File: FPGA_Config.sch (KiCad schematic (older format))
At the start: 27 parts, among them J1 104031-0811, U1 XA7Z020-1CLG400Q

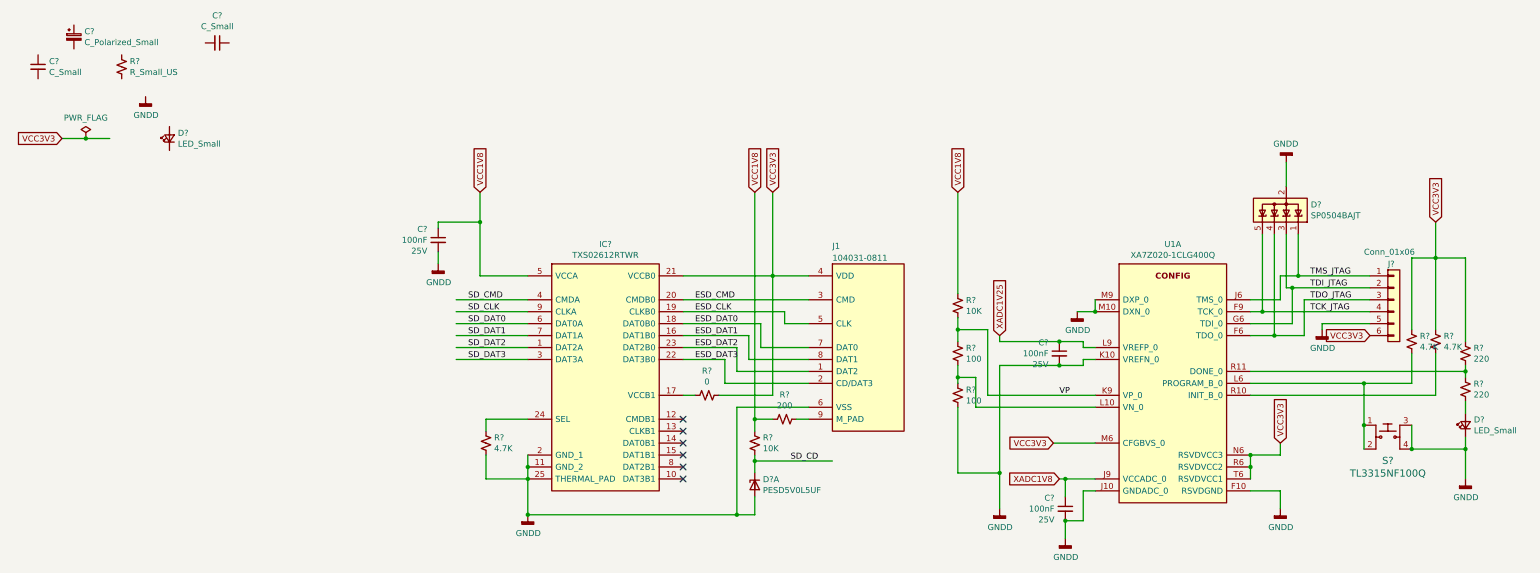
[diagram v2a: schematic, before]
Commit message: PCB created and schematics annotated High speed connections added to the BTB
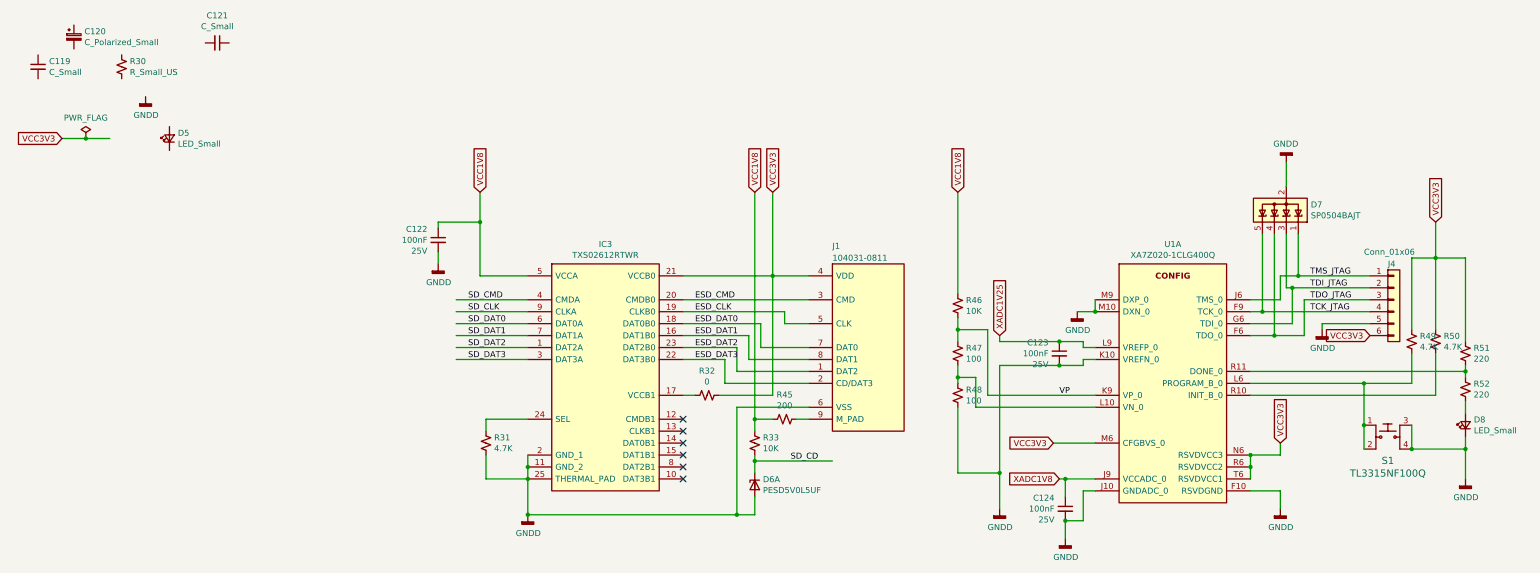
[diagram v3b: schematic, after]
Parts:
- gave numbers to parts that had none: 25

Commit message: Corrected PCB import errors
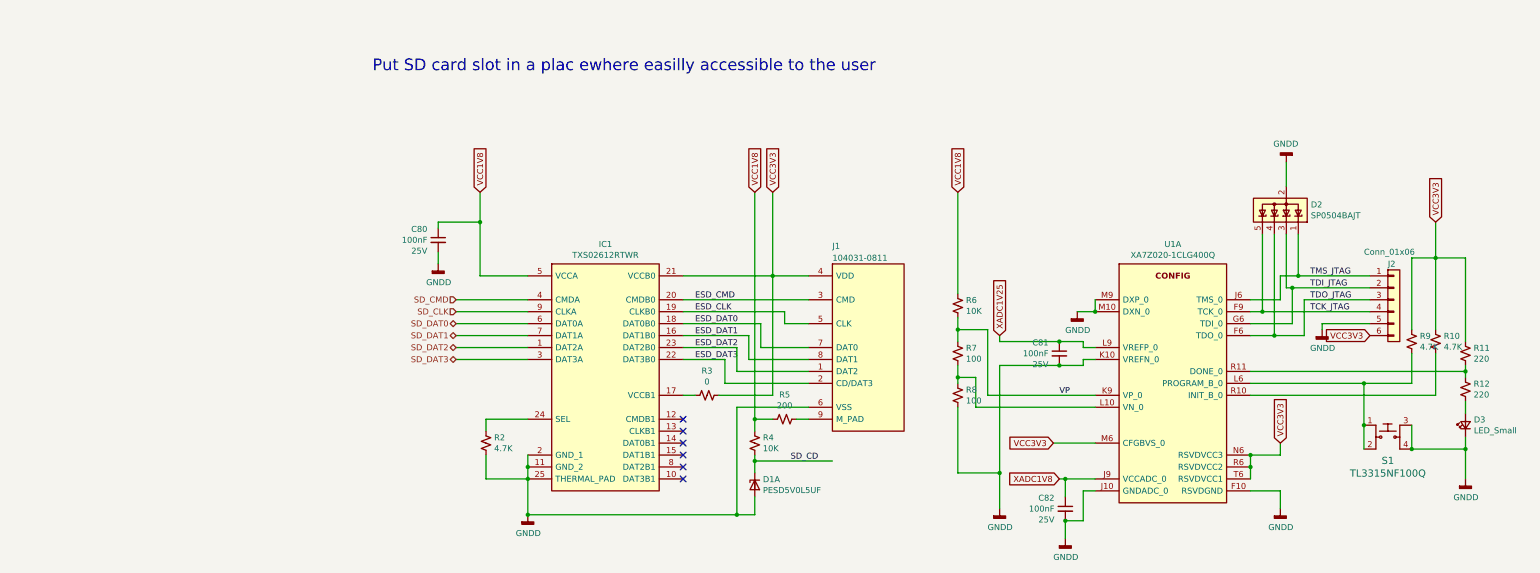
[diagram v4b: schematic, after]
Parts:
- removed C119: C_Small, Capacitor_SMD:C_0603_1608Metric_Pad1.08x0.95mm_HandSolder, symbol Device:C_Small
- removed C120: C_Polarized_Small, Capacitor_Tantalum_SMD:CP_EIA-1608-10_AVX-L_Pad1.25x1.05mm_HandSolder, symbol Device:C_Polarized_Small
- removed C121: C_Small, symbol Device:C_Small
- removed D5: LED_Small, symbol Device:LED_Small
- removed R30: R_Small_US, Resistor_SMD:R_0603_1608Metric_Pad0.98x0.95mm_HandSolder, symbol Device:R_Small_US
- D3: renamed from D8; footprint (none) -> LED_SMD:LED_0603_1608Metric
- J2: renamed from J4; footprint (none) -> Connector_PinHeader_2.54mm:PinHeader_1x06_P2.54mm_Vertical
- renumbered C122 to C80, C123 to C81, C124 to C82, D6 to D1, D7 to D2, IC3 to IC1, R50 to R10, R51 to R11, R52 to R12, R31 to R2, R32 to R3, R33 to R4, R45 to R5, R46 to R6, R47 to R7, R48 to R8, R49 to R9
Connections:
- wire segments 137 -> 135
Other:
- note added: "Put SD card slot in a plac ewhere easilly accessible to the user"
